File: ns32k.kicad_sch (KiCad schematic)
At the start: 41 parts, among them U1 NS32201, U10 74AHC373, U11 74AHC373, U12 74AHC138, U13 AS6C6416-55, U15 MX29LV040C, U16 MX29LV040C, U3 NS32016, U4 NS32082, U5 NS32202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

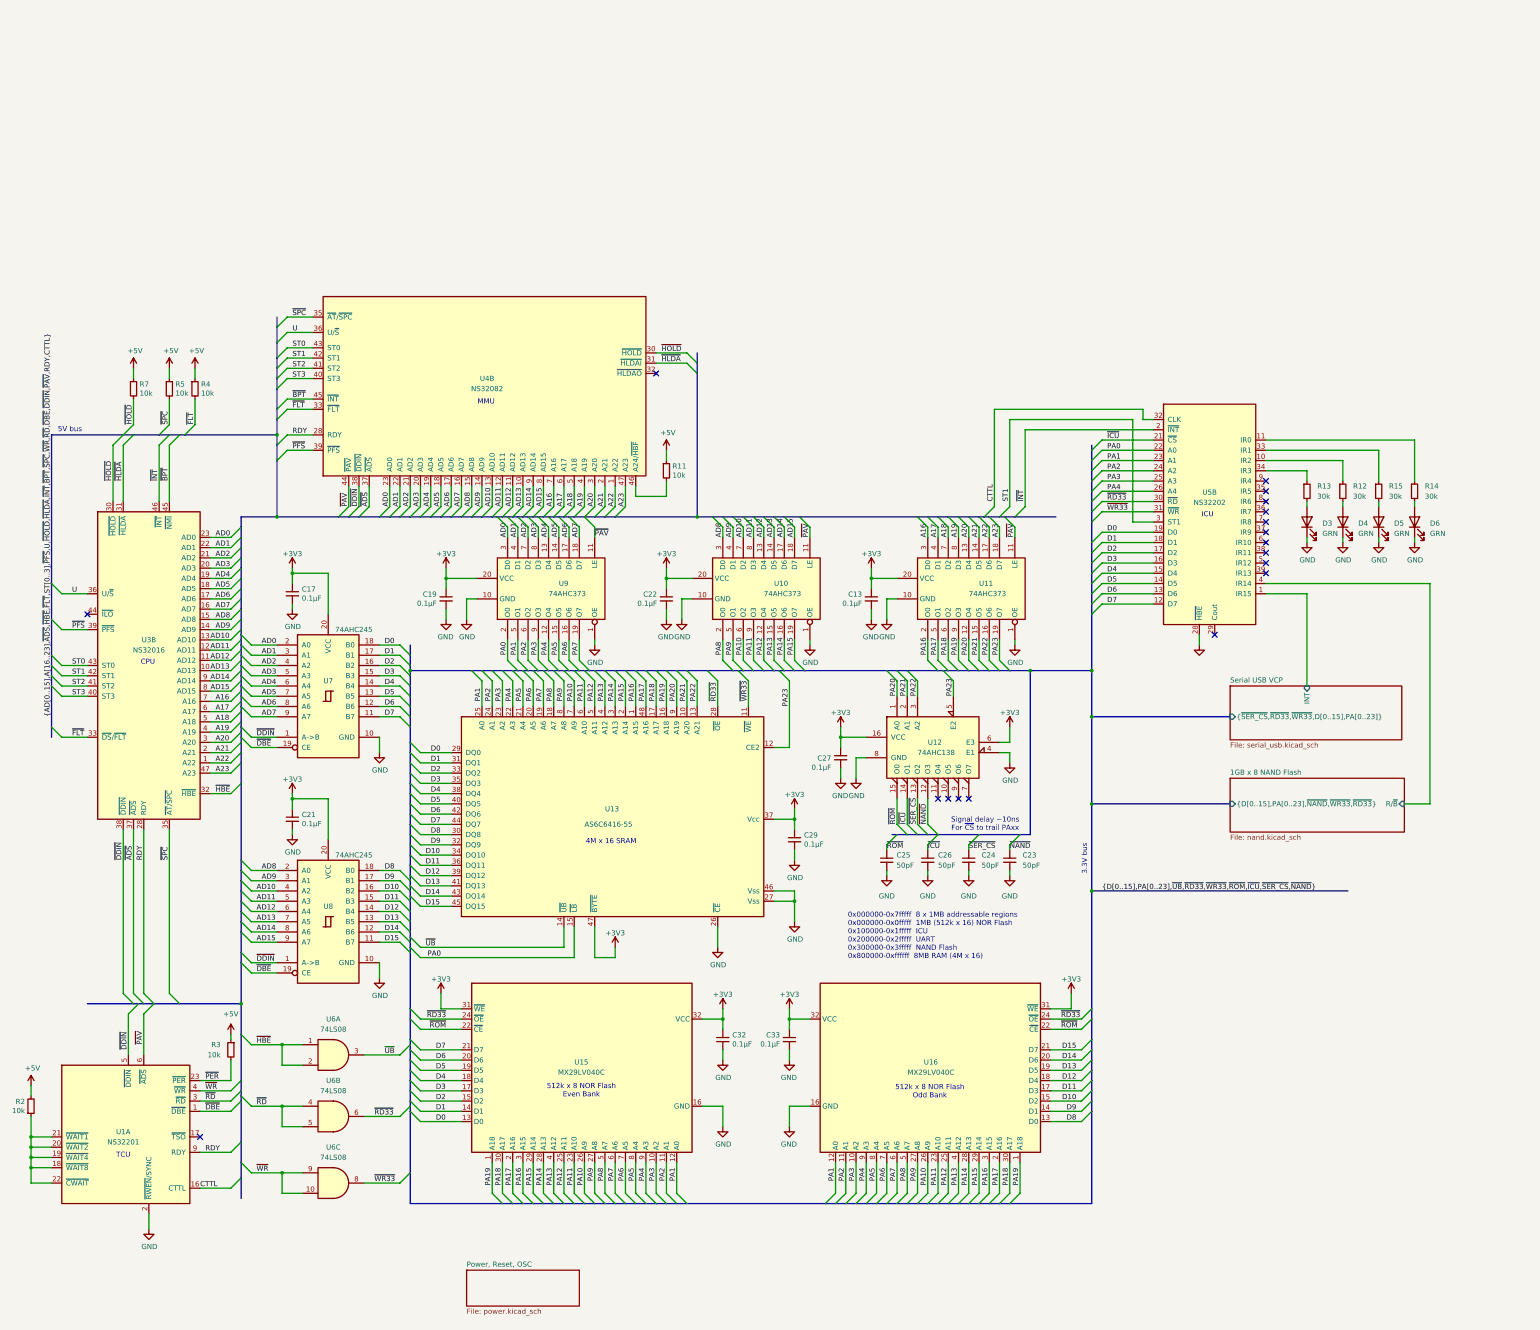
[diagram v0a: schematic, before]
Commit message: add ICU int ack decoding
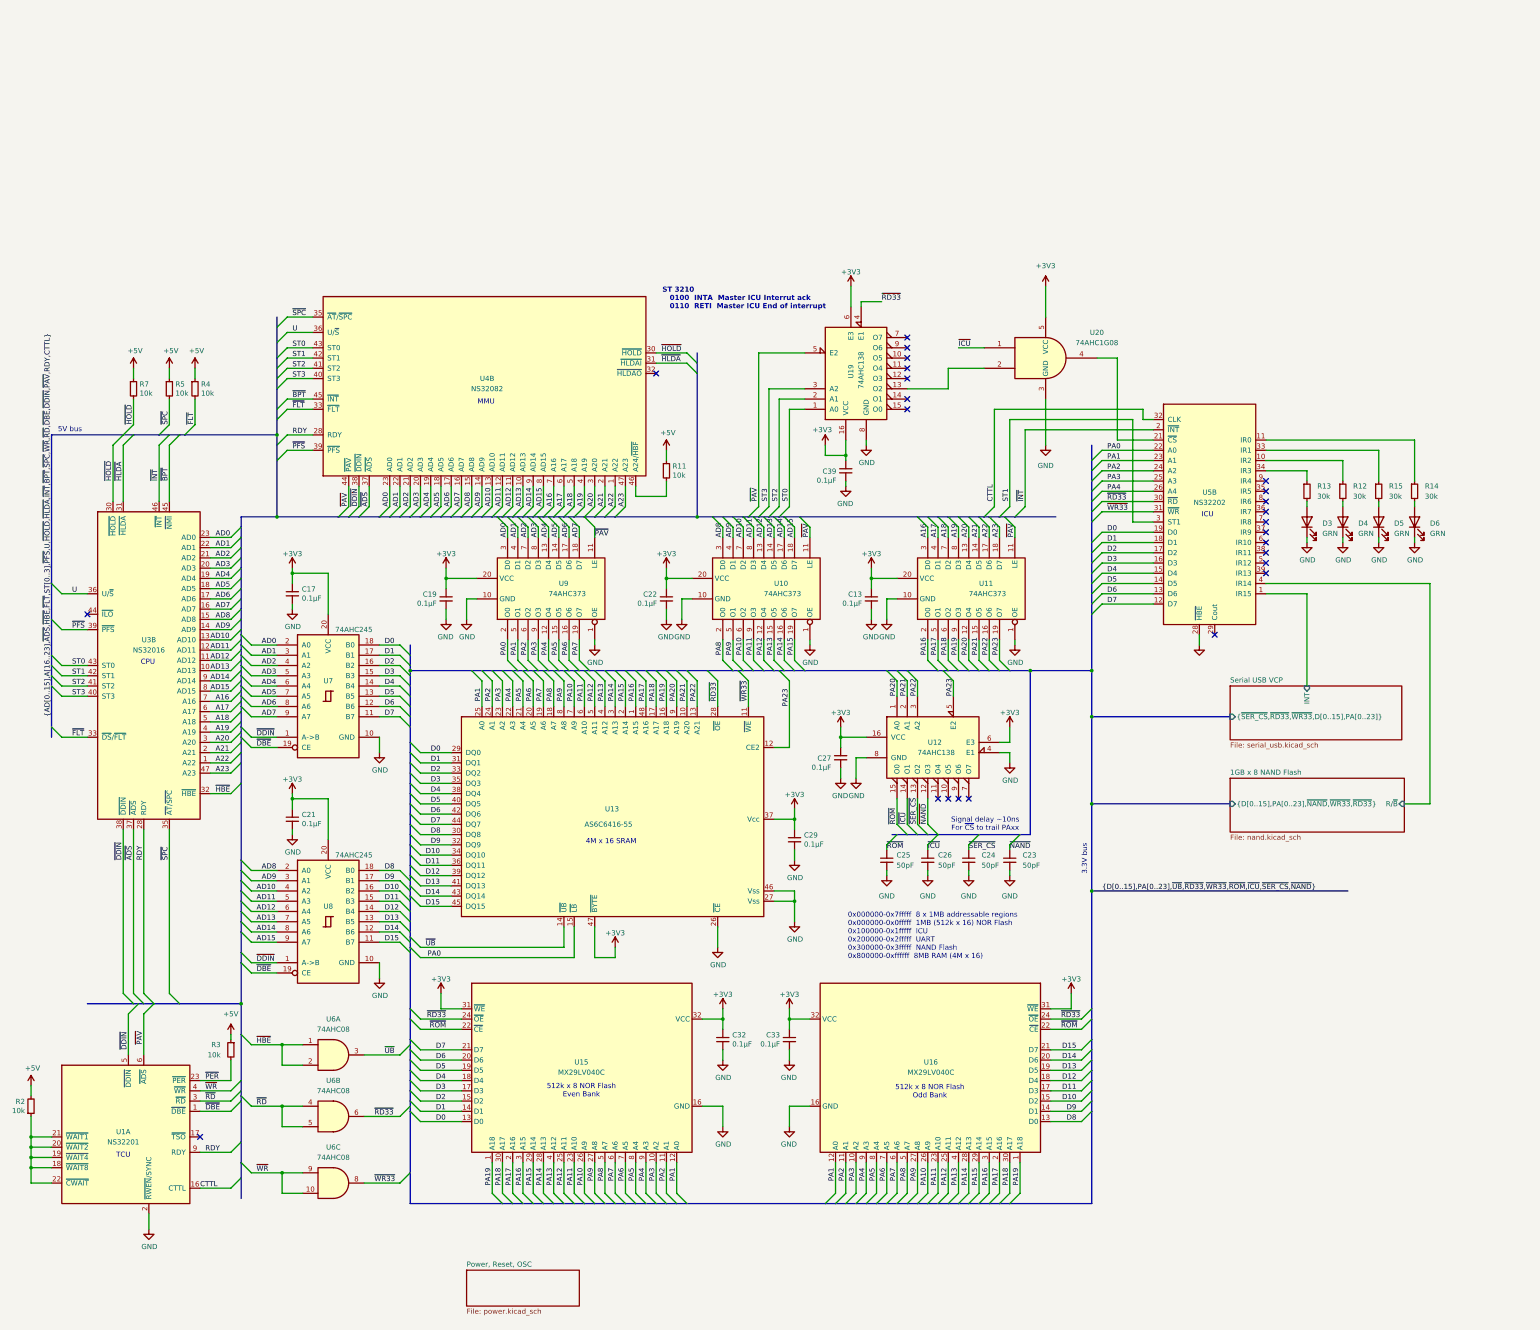
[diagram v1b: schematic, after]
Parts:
- added C39: 0.1µF, Capacitor_SMD:C_0402_1005Metric, symbol Device:C_Small
- added U19: 74AHC138, Package_SO:TSSOP-16_4.4x5mm_P0.65mm, symbol 74AHC138:74AHC138
- added U20: 74AHC1G08, Package_TO_SOT_SMD:SOT-23-5, symbol 74xGxx:74AHC1G08
- U6: value 74LS08 -> 74AHC08
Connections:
- net +3V3: now also C39.1, U19.16 (VCC), U19.6 (E3), U20.5 (VCC)
- net GND: now also C39.2, U19.8 (GND), U20.3 (GND)
- net ST0: now also U19.1 (A0)
- net ST2: now also U19.2 (A1)
- net ST3: now also U19.3 (A2)
- net ~{ICU}: now also U20.1; no longer U5.21 (~{CS})
- net ~{PAV}: now also U19.5 (E2)
- net ~{RD33}: now also U19.4 (E1)
- new net: U19.13 (O2), U20.2
- new net: U20.4, U5.21 (~{CS})
- no-connect marks 18 -> 25
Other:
- note added: "ST 3210 0100 INTA Master ICU Interrut ack 0110 RETI Master ICU End of interrupt"

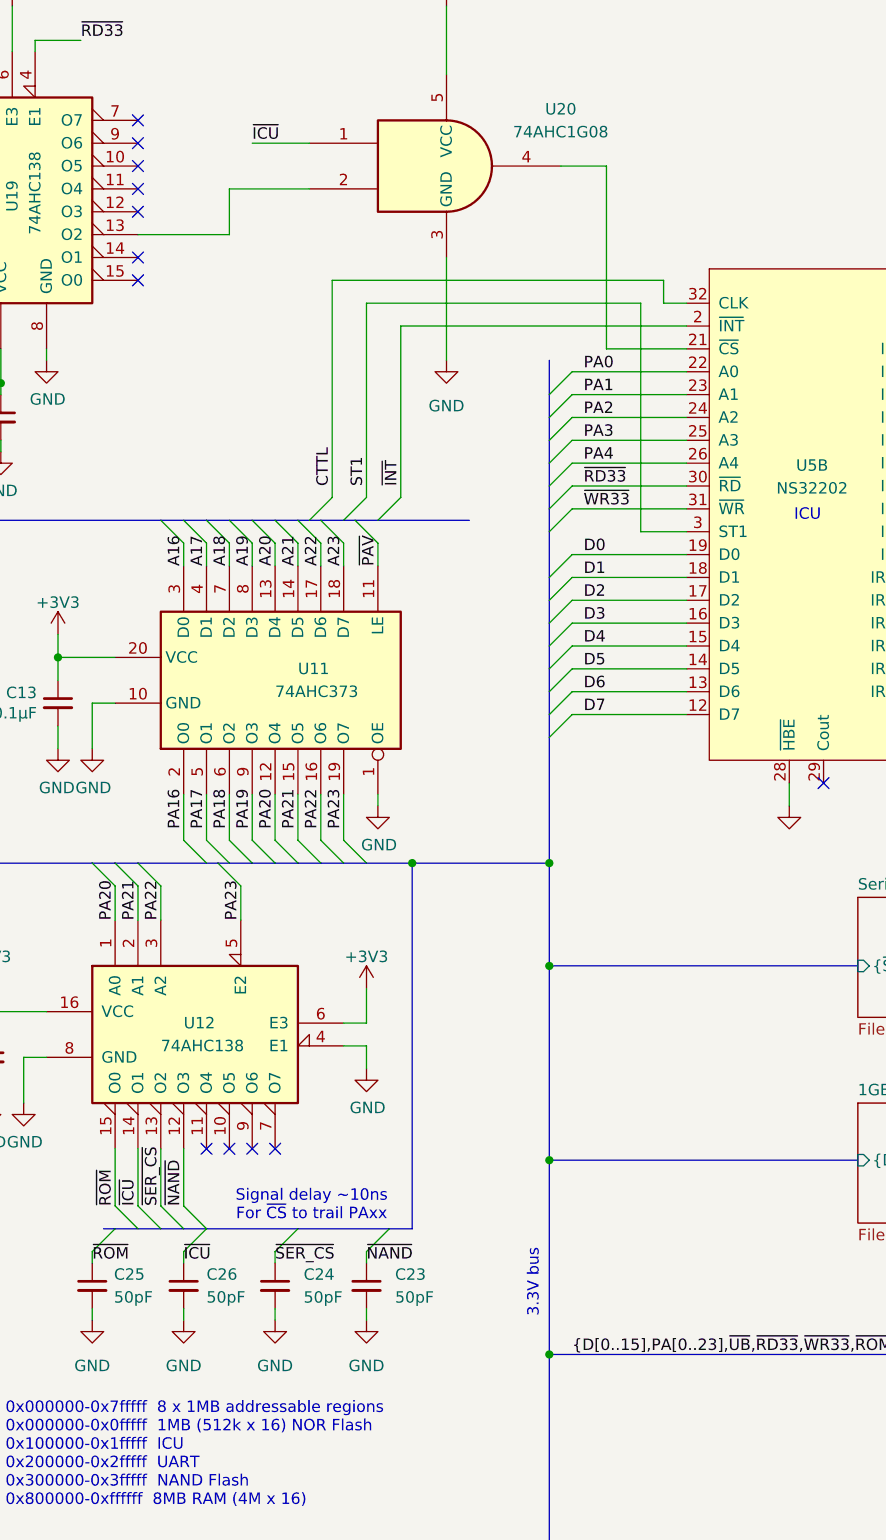
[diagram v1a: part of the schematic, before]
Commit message: move ICU# delay to after decode
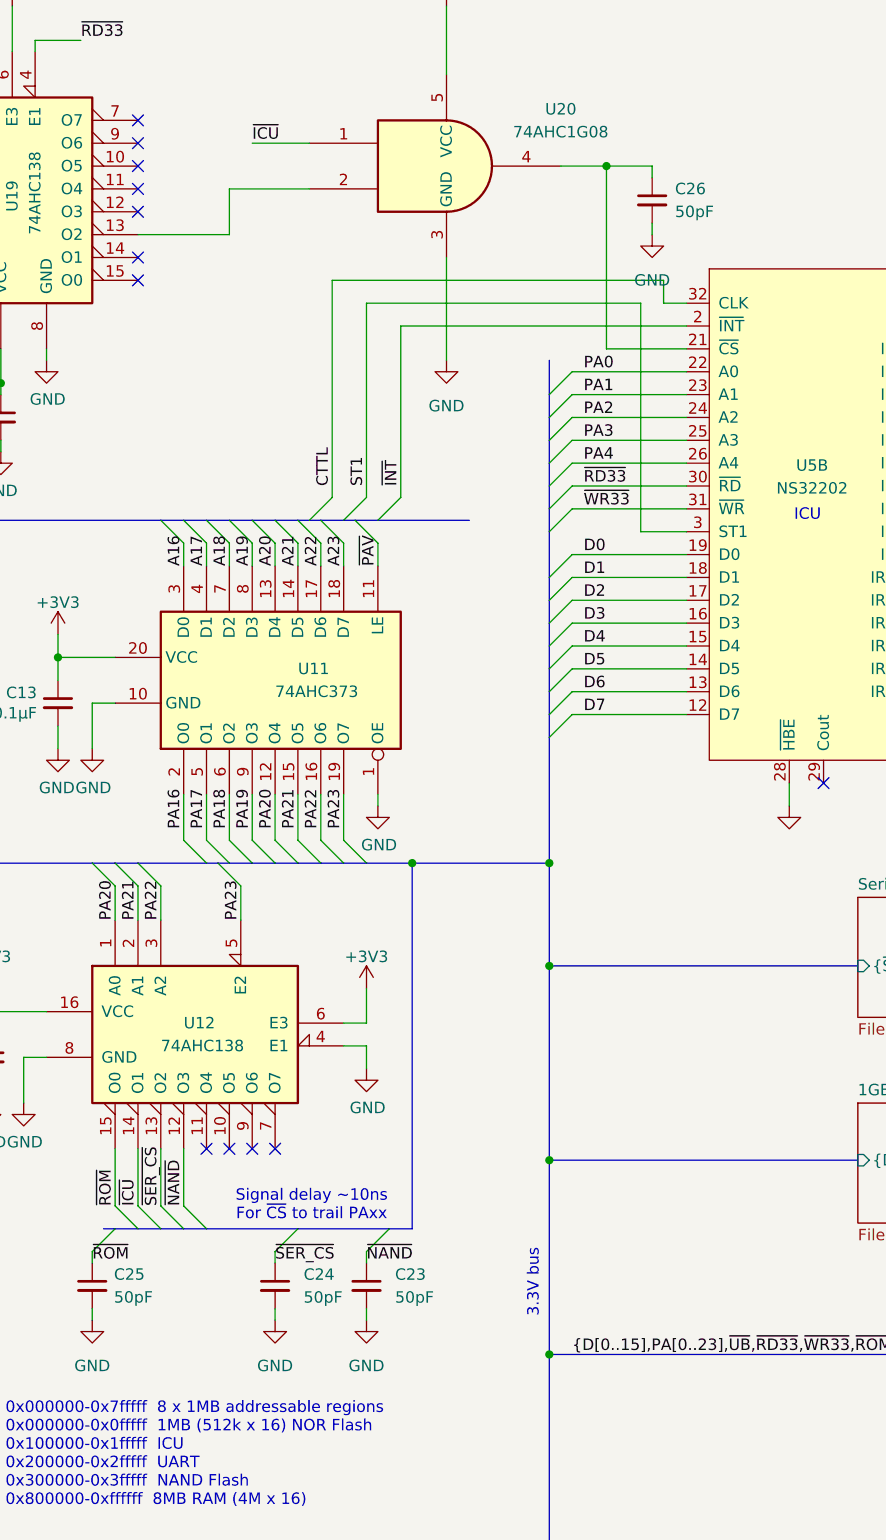
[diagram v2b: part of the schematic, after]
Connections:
- net ~{ICU}: no longer C26.1
- net at U20.4, U5.21 (~{CS}): now also C26.1
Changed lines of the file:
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@@
 	(title_block
 		(title "NS32016 Toy PCB")
-		(date "2024-07-19")
-		(rev "Rev 1")
+		(date "2024-07-24")
+		(rev "Rev 2")
 		(comment 1 "bson@rockgarden.net")
 		(comment 2 "Jan Brittenson")
@@
 	)
 	(junction
+		(at 299.72 36.83)
+		(diameter 0)
+		(color 0 0 0 0)
+	)
+	(junction
 		(at 293.37 114.3)
 		(diameter 0)
@@
 	)
 	(bus_entry
-		(at 255.27 154.94)
-		(size -2.54 2.54)
-		(stroke
-			(width 0)
-			(type default)
-		)
-	)
-	(bus_entry
 		(at 270.51 246.38)
 		(size 2.54 -2.54)
@@
 	(wire
 		(pts
-			(xy 252.73 163.83) (xy 252.73 165.1)
-		)
-		(stroke
-			(width 0)
-			(type default)
-		)
-	)
-	(wire
-		(pts
 			(xy 127 170.18) (xy 134.62 170.18)
 		)
@@
 	(wire
 		(pts
+			(xy 304.8 36.83) (xy 304.8 38.1)
+		)
+		(stroke
+			(width 0)
+			(type default)
+		)
+	)
+	(wire
+		(pts
 			(xy 95.25 88.9) (xy 95.25 90.17)
 		)
@@
 	(wire
 		(pts
+			(xy 304.8 43.18) (xy 304.8 44.45)
+		)
+		(stroke
+			(width 0)
+			(type default)
+		)
+	)
+	(wire
+		(pts
 			(xy 172.72 243.84) (xy 172.72 236.22)
 		)
@@
 	(wire
 		(pts
-			(xy 252.73 157.48) (xy 252.73 158.75)
-		)
-		(stroke
-			(width 0)
-			(type default)
-		)
-	)
-	(wire
-		(pts
 			(xy 201.93 111.76) (xy 201.93 106.68)
 		)
@@
 	(wire
 		(pts
+			(xy 299.72 36.83) (xy 304.8 36.83)
+		)
+		(stroke
+			(width 0)
+			(type default)
+		)
+	)
+	(wire
+		(pts
 			(xy 127 73.66) (xy 127 68.58)
 		)
@@
 		)
 	)
-	(label "~{ICU}"
-		(at 252.73 158.75 0)
-		(fields_autoplaced yes)
-		(effects
-			(font
-				(size 1.27 1.27)
-			)
-			(justify left bottom)
-		)
-	)
 	(label "A19"
 		(at 260.35 81.28 90)
@@
 	)
 	(symbol
-		(lib_id "power:GND")
-		(at 252.73 165.1 0)
-		(unit 1)
-		(exclude_from_sim no)
-		(in_bom yes)
-		(on_board yes)
-		(dnp no)
-		(fields_autoplaced yes)
-		(property "Reference" "#PWR041"
-			(at 252.73 171.45 0)
-			(effects
-				(font
-					(size 1.27 1.27)
-				)
-				(hide yes)
-			)
-		)
-		(property "Value" "GND"
-			(at 252.73 170.18 0)
-			(effects
-				(font
-					(size 1.27 1.27)
-				)
-			)
-		)
-		(property "Footprint" ""
-			(at 252.73 165.1 0)
-			(effects
-				(font
-					(size 1.27 1.27)
-				)
-				(hide yes)
-			)
-		)
-		(property "Datasheet" ""
-			(at 252.73 165.1 0)
-			(effects
-				(font
-					(size 1.27 1.27)
-				)
-				(hide yes)
-			)
-		)
-		(property "Description" "Power symbol creates a global label with name \"GND\" , ground"
-			(at 252.73 165.1 0)
-			(effects
-				(font
-					(size 1.27 1.27)
-				)
-				(hide yes)
-			)
-		)
-		(pin "1"
-		)
-		(instances
-			(project "ns32k"
-				(path "/54787df0-1b8c-465f-acae-f55ec7f02da3"
-					(reference "#PWR041")
-					(unit 1)
-				)
-			)
-		)
-	)
-	(symbol
 		(lib_id "74xGxx:74AHC1G08")
 		(at 281.94 36.83 0)
@@
 	)
 	(symbol
+		(lib_id "power:GND")
+		(at 304.8 44.45 0)
+		(unit 1)
+		(exclude_from_sim no)
+		(in_bom yes)
+		(on_board yes)
+		(dnp no)
+		(fields_autoplaced yes)
+		(property "Reference" "#PWR041"
+			(at 304.8 50.8 0)
+			(effects
+				(font
+					(size 1.27 1.27)
+				)
+				(hide yes)
+			)
+		)
+		(property "Value" "GND"
+			(at 304.8 49.53 0)
+			(effects
+				(font
+					(size 1.27 1.27)
+				)
+			)
+		)
+		(property "Footprint" ""
+			(at 304.8 44.45 0)
+			(effects
+				(font
+					(size 1.27 1.27)
+				)
+				(hide yes)
+			)
+		)
+		(property "Datasheet" ""
+			(at 304.8 44.45 0)
+			(effects
+				(font
+					(size 1.27 1.27)
+				)
+				(hide yes)
+			)
+		)
+		(property "Description" "Power symbol creates a global label with name \"GND\" , ground"
+			(at 304.8 44.45 0)
+			(effects
+				(font
+					(size 1.27 1.27)
+				)
+				(hide yes)
+			)
+		)
+		(pin "1"
+		)
+		(instances
+			(project "ns32k"
+				(path "/54787df0-1b8c-465f-acae-f55ec7f02da3"
+					(reference "#PWR041")
+					(unit 1)
+				)
+			)
+		)
+	)
+	(symbol
 		(lib_id "Device:R_Small")
 		(at 355.6 69.85 0)
@@
 	)
 	(symbol
-		(lib_id "Device:C_Small")
-		(at 252.73 161.29 0)
-		(unit 1)
-		(exclude_from_sim no)
-		(in_bom yes)
-		(on_board yes)
-		(dnp no)
-		(property "Reference" "C26"
-			(at 255.27 160.02 0)
-			(effects
-				(font
-					(size 1.27 1.27)
-				)
-				(justify left)
-			)
-		)
-		(property "Value" "50pF"
-			(at 255.27 162.56 0)
-			(effects
-				(font
-					(size 1.27 1.27)
-				)
-				(justify left)
-			)
-		)
-		(property "Footprint" "Capacitor_SMD:C_0402_1005Metric"
-			(at 252.73 161.29 0)
-			(effects
-				(font
-					(size 1.27 1.27)
-				)
-				(hide yes)
-			)
-		)
-		(property "Datasheet" "~"
-			(at 252.73 161.29 0)
-			(effects
-				(font
-					(size 1.27 1.27)
-				)
-				(hide yes)
-			)
-		)
-		(property "Description" "Unpolarized capacitor, small symbol"
-			(at 252.73 161.29 0)
-			(effects
-				(font
-					(size 1.27 1.27)
-				)
-				(hide yes)
-			)
-		)
-		(pin "1"
-		)
-		(pin "2"
-		)
-		(instances
-			(project "ns32k"
-				(path "/54787df0-1b8c-465f-acae-f55ec7f02da3"
-					(reference "C26")
-					(unit 1)
-				)
-			)
-		)
-	)
-	(symbol
 		(lib_id "power:+3V3")
 		(at 218.44 198.12 0)
@@
 					(unit 1)
 				)
+			)
+		)
+	)
+	(symbol
+		(lib_id "Device:C_Small")
+		(at 304.8 40.64 0)
+		(unit 1)
+		(exclude_from_sim no)
+		(in_bom yes)
+		(on_board yes)
+		(dnp no)
+		(property "Reference" "C26"
+			(at 307.34 39.37 0)
+			(effects
+				(font
+					(size 1.27 1.27)
+				)
+				(justify left)
+			)
+		)
+		(property "Value" "50pF"
+			(at 307.34 41.91 0)
+			(effects
+				(font
+					(size 1.27 1.27)
+				)
+				(justify left)
+			)
+		)
+		(property "Footprint" "Capacitor_SMD:C_0402_1005Metric"
+			(at 304.8 40.64 0)
+			(effects
+				(font
+					(size 1.27 1.27)
+				)
+				(hide yes)
+			)
+		)
+		(property "Datasheet" "~"
+			(at 304.8 40.64 0)
+			(effects
+				(font
+					(size 1.27 1.27)
+				)
+				(hide yes)
+			)
+		)
+		(property "Description" "Unpolarized capacitor, small symbol"
+			(at 304.8 40.64 0)
+			(effects
+				(font
+					(size 1.27 1.27)
+				)
+				(hide yes)
+			)
+		)
+		(pin "1"
+		)
+		(pin "2"
+		)
+		(instances
+			(project "ns32k"
+				(path "/54787df0-1b8c-465f-acae-f55ec7f02da3"
+					(reference "C26")
+					(unit 1)
+				)

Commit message: cleanups, DRC
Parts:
- added R26, R27, R28, R29: 30k, Resistor_SMD:R_0402_1005Metric, symbol Device:R_Small
- added SW2: SW_DIP_x04, Button_Switch_SMD:SW_DIP_SPSTx04_Slide_Copal_CHS-04B_W7.62mm_P1.27mm, symbol Switch:SW_DIP_x04
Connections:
- net +5V: now also R26.1, R27.1, R28.1, R29.1
- net GND: now also SW2.5, SW2.6, SW2.7, SW2.8
- net at U5.35 (IR5): now also R27.2, SW2.2
- net at U5.36 (IR7): now also R29.2, SW2.4
- net at U5.8 (IR6): now also R28.2, SW2.3
- net at U5.9 (IR4): now also R26.2, SW2.1
- no-connect marks 25 -> 21
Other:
- moved on the sheet: D3, D4, D5, D6, R12, R13, R14, R15
